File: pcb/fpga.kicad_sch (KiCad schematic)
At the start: 20 parts, among them J13 KB, J5 FPGA JTAG, J7 RAM cacheable, J8 ROM cacheable, U2 XC2S100TQ144, Y1 TXC-7C, Y2 GTXO-14T

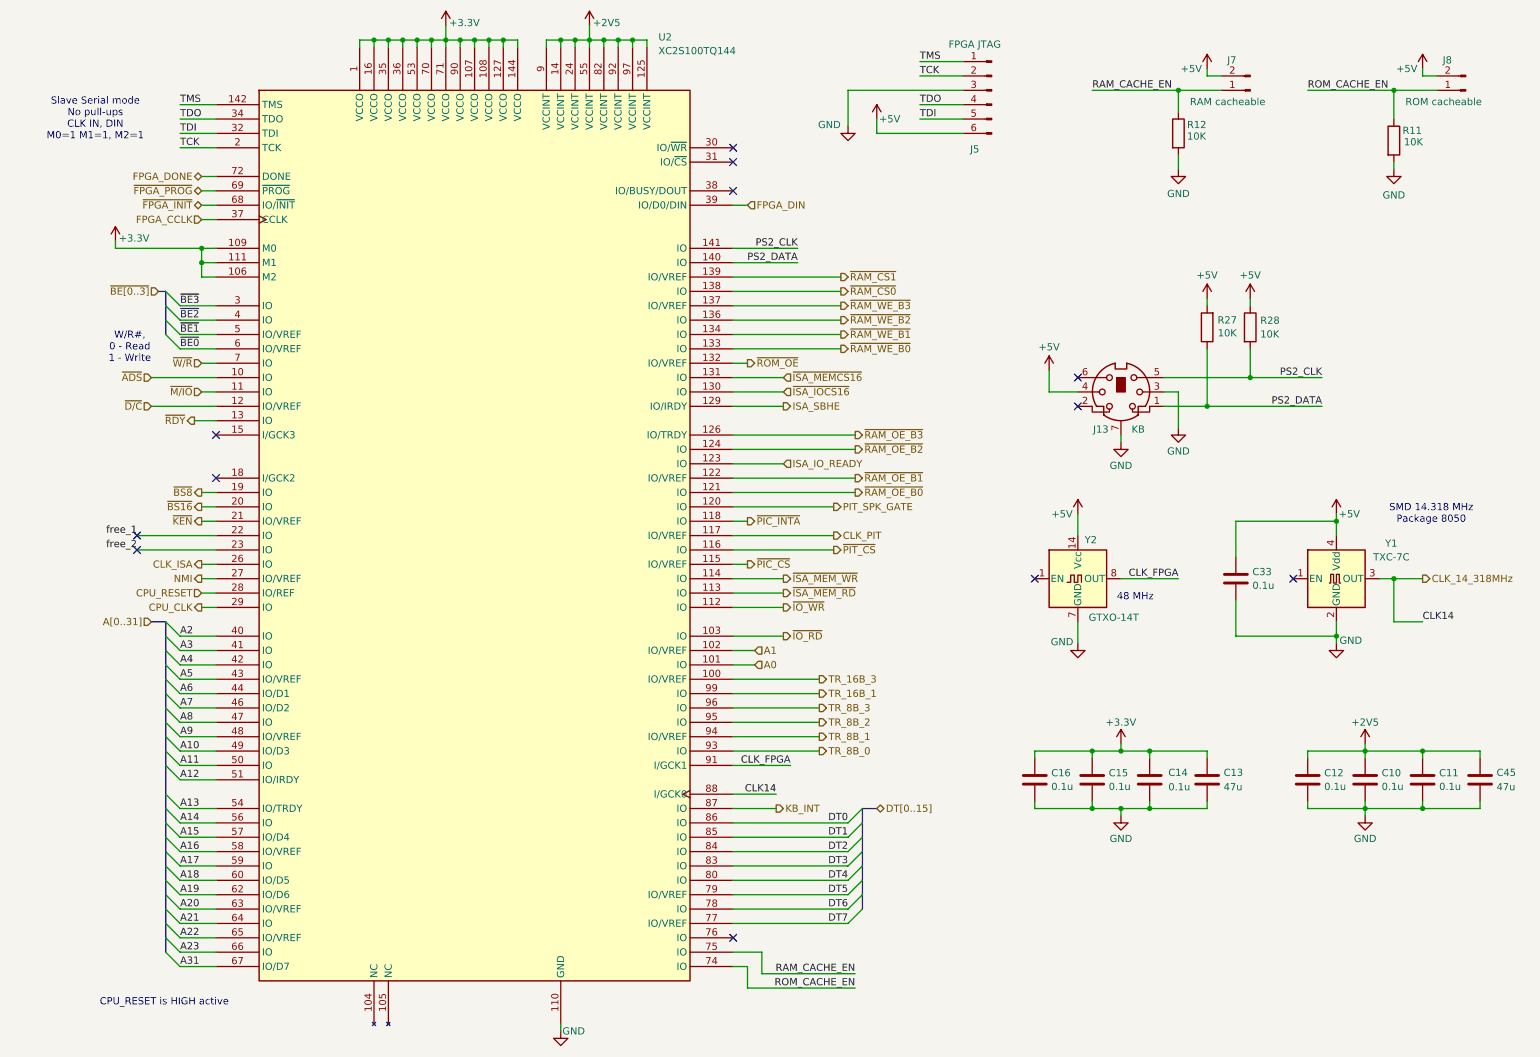
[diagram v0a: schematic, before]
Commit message: reshuffling FPGA diagram IO for better PCB routing, removed RAM/ROM CACHE_EN jumpers, 10 spare FPGA IO free. Replaced JTAG header with smaller probe points.
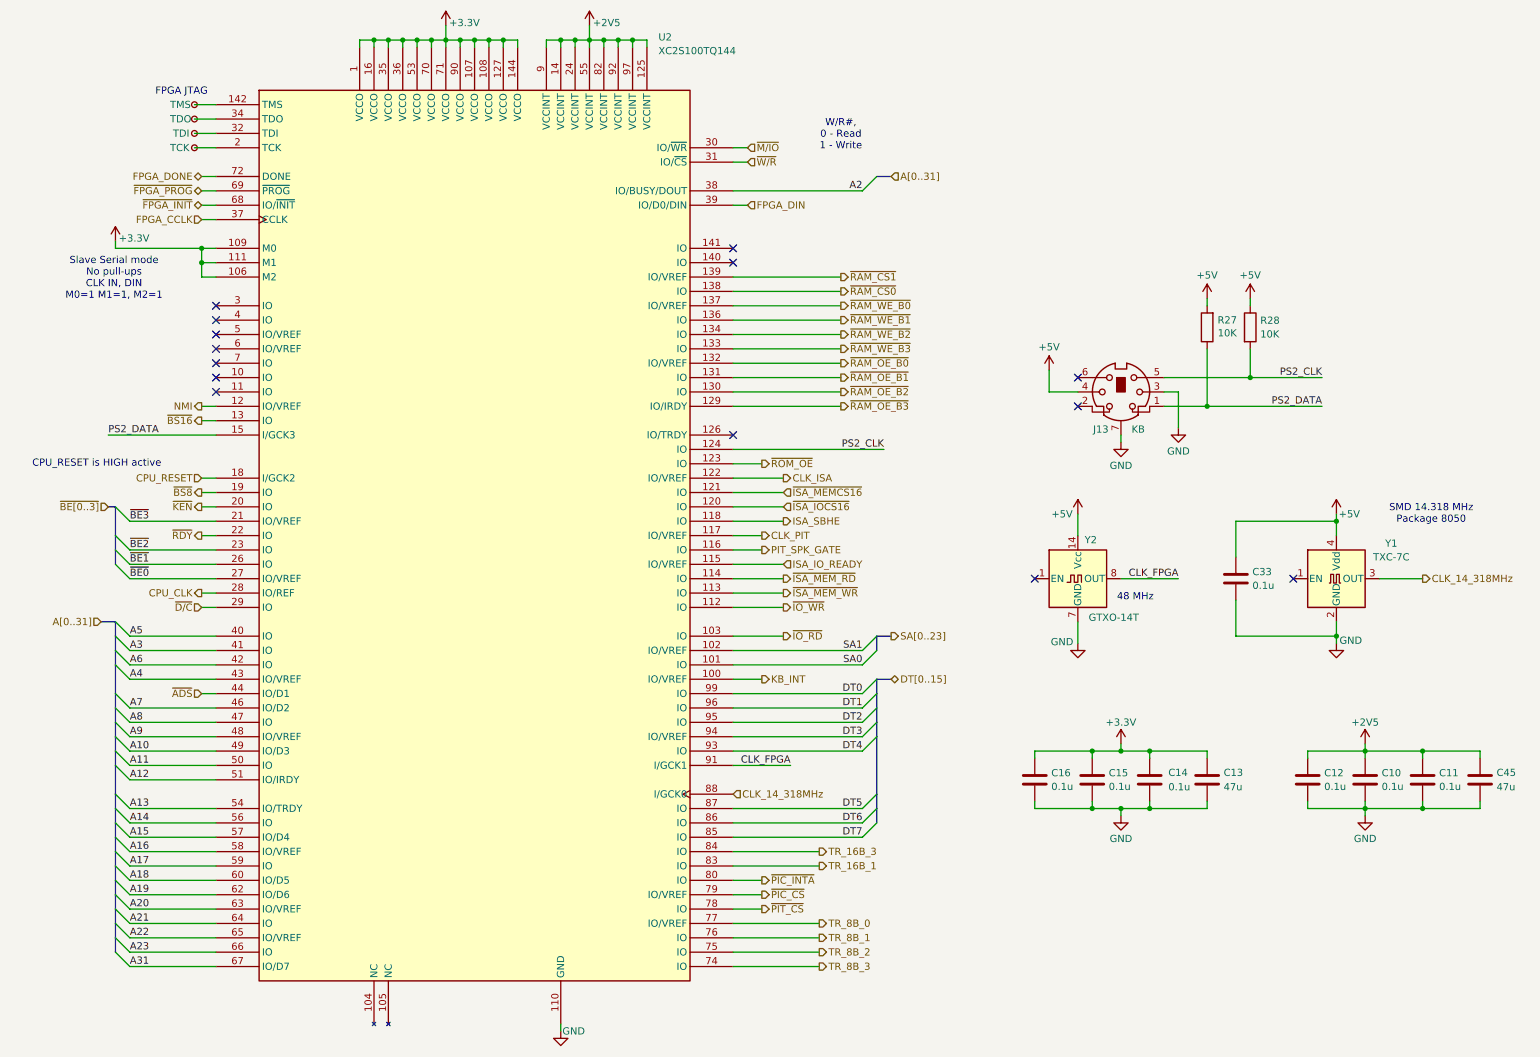
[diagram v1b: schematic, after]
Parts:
- removed J5: FPGA JTAG, Connector_PinHeader_2.54mm:PinHeader_1x06_P2.54mm_Vertical, symbol Connector:Conn_01x06_Pin
- removed J7: RAM cacheable, Connector_PinHeader_2.54mm:PinHeader_1x02_P2.54mm_Vertical, symbol Connector:Conn_01x02_Pin
- removed J8: ROM cacheable, Connector_PinHeader_2.54mm:PinHeader_1x02_P2.54mm_Vertical, symbol Connector:Conn_01x02_Pin
- removed R11, R12: 10K, Resistor_SMD:R_0805_2012Metric_Pad1.20x1.40mm_HandSolder, symbol Device:R
- added TP1: TDO, 486custom:TestPoint_Pad_D0.4mm, symbol Connector:TestPoint_Small
- added TP2: TDI, 486custom:TestPoint_Pad_D0.4mm, symbol Connector:TestPoint_Small
- added TP3: TMS, 486custom:TestPoint_Pad_D0.4mm, symbol Connector:TestPoint_Small
- added TP4: TCK, 486custom:TestPoint_Pad_D0.4mm, symbol Connector:TestPoint_Small
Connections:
- net RAM_CACHE_EN is gone; now on net TR_8B_2: U2.75 (IO)
- net ROM_CACHE_EN is gone; now on net TR_8B_3: U2.74 (IO)
- net free_1 is gone; now on net ~{RDY}: U2.22 (IO)
- net free_2 is gone; now on net ~{BE2}: U2.23 (IO)
- net A2: now also U2.38 (IO/BUSY/DOUT); no longer U2.40 (IO)
- net A4: now also U2.43 (IO/VREF); no longer U2.42 (IO)
- net A5: now also U2.40 (IO); no longer U2.43 (IO/VREF)
- net A6: now also U2.42 (IO); no longer U2.44 (IO/D1)
- net CLK_ISA: now also U2.122 (IO/VREF); no longer U2.26 (IO)
- net CPU_CLK: now also U2.28 (IO/REF); no longer U2.29 (IO)
- net CPU_RESET: now also U2.18 (I/GCK2); no longer U2.28 (IO/REF)
- net DT0: now also U2.99 (IO); no longer U2.86 (IO)
- net DT1: now also U2.96 (IO); no longer U2.85 (IO)
- net DT2: now also U2.95 (IO); no longer U2.84 (IO)
- net DT3: now also U2.94 (IO/VREF); no longer U2.83 (IO)
- net DT4: now also U2.93 (IO); no longer U2.80 (IO)
- net DT5: now also U2.87 (IO); no longer U2.79 (IO/VREF)
- net DT6: now also U2.86 (IO); no longer U2.78 (IO)
- net DT7: now also U2.85 (IO); no longer U2.77 (IO/VREF)
- net ISA_IO_READY: now also U2.115 (IO/VREF); no longer U2.123 (IO)
- net ISA_SBHE: now also U2.118 (IO); no longer U2.129 (IO/IRDY)
- net KB_INT: now also U2.100 (IO/VREF); no longer U2.87 (IO)
- net NMI: now also U2.12 (IO/VREF); no longer U2.27 (IO/VREF)
- net PIT_SPK_GATE: now also U2.116 (IO); no longer U2.120 (IO)
- net PS2_CLK: now also U2.124 (IO); no longer U2.141 (IO)
- net PS2_DATA: now also U2.15 (I/GCK3); no longer U2.140 (IO)
- net TR_16B_1: now also U2.83 (IO); no longer U2.99 (IO)
- net TR_16B_3: now also U2.84 (IO); no longer U2.100 (IO/VREF)
- net TR_8B_0: now also U2.77 (IO/VREF); no longer U2.93 (IO)
- net TR_8B_1: now also U2.76 (IO); no longer U2.94 (IO/VREF)
- net TR_8B_2: no longer U2.95 (IO)
- net TR_8B_3: no longer U2.96 (IO)
- net ~{ADS}: now also U2.44 (IO/D1); no longer U2.10 (IO)
- net ~{BE0}: now also U2.27 (IO/VREF); no longer U2.6 (IO/VREF)
- net ~{BE1}: now also U2.26 (IO); no longer U2.5 (IO/VREF)
- net ~{BE2}: no longer U2.4 (IO)
- net ~{BE3}: now also U2.21 (IO/VREF); no longer U2.3 (IO)
- net ~{BS16}: now also U2.13 (IO); no longer U2.20 (IO)
- net ~{D/C}: now also U2.29 (IO); no longer U2.12 (IO/VREF)
- net ~{ISA_IOCS16}: now also U2.120 (IO); no longer U2.130 (IO)
- net ~{ISA_MEMCS16}: now also U2.121 (IO); no longer U2.131 (IO)
- net ~{ISA_MEM_RD}: now also U2.114 (IO); no longer U2.113 (IO)
- net ~{ISA_MEM_WR}: now also U2.113 (IO); no longer U2.114 (IO)
- net ~{KEN}: now also U2.20 (IO); no longer U2.21 (IO/VREF)
- net ~{M/IO}: now also U2.30 (IO/~{WR}); no longer U2.11 (IO)
- net ~{PIC_CS}: now also U2.79 (IO/VREF); no longer U2.115 (IO/VREF)
- net ~{PIC_INTA}: now also U2.80 (IO); no longer U2.118 (IO)
- net ~{PIT_CS}: now also U2.78 (IO); no longer U2.116 (IO)
- net ~{RAM_OE_B0}: now also U2.132 (IO/VREF); no longer U2.121 (IO)
- net ~{RAM_OE_B1}: now also U2.131 (IO); no longer U2.122 (IO/VREF)
- net ~{RAM_OE_B2}: now also U2.130 (IO); no longer U2.124 (IO)
- net ~{RAM_OE_B3}: now also U2.129 (IO/IRDY); no longer U2.126 (IO/TRDY)
- net ~{RAM_WE_B0}: now also U2.137 (IO/VREF); no longer U2.133 (IO)
- net ~{RAM_WE_B1}: now also U2.136 (IO); no longer U2.134 (IO)
- net ~{RAM_WE_B2}: now also U2.134 (IO); no longer U2.136 (IO)
- net ~{RAM_WE_B3}: now also U2.133 (IO); no longer U2.137 (IO/VREF)
- net ~{RDY}: no longer U2.13 (IO)
- net ~{ROM_OE}: now also U2.123 (IO); no longer U2.132 (IO/VREF)
- net ~{W/R}: now also U2.31 (IO/~{CS}); no longer U2.7 (IO)
- net A0 renamed SA0
- net A1 renamed SA1
- net TCK: no longer names the net of U2.2 (TCK)
- net TCK: now also TP4.1
- net TDI: no longer names the net of U2.32 (TDI)
- net TDI: now also TP2.1
- net TDO: no longer names the net of U2.34 (TDO)
- net TDO: now also TP1.1
- net TMS: no longer names the net of U2.142 (TMS)
- net TMS: now also TP3.1
- no-connect marks 12 -> 14
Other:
- note added: "FPGA JTAG"

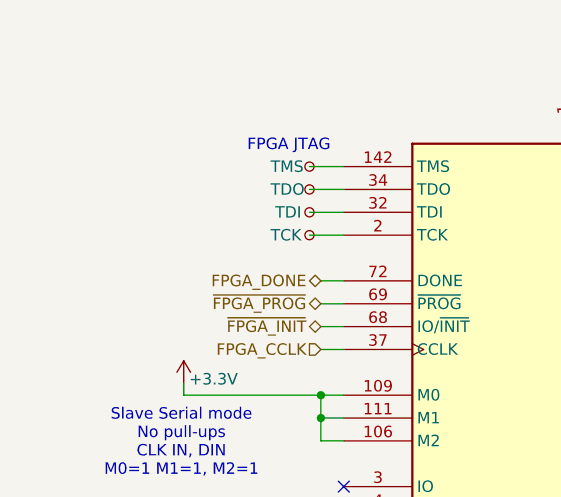
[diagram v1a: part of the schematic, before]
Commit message: fpga diagram extra JTAG ground point
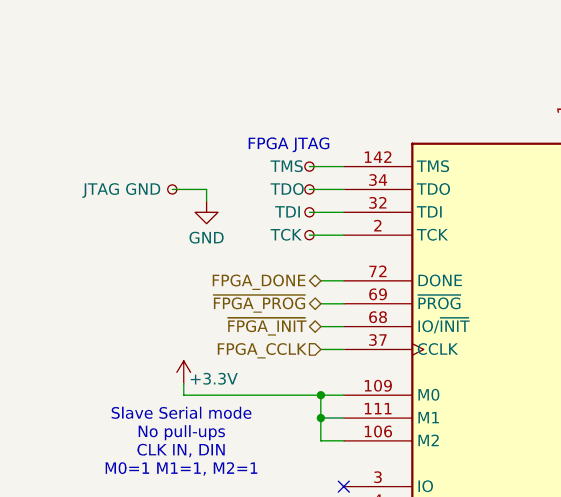
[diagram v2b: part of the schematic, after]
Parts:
- added TP5: JTAG GND, 486custom:TestPoint_Pad_D0.4mm, symbol Connector:TestPoint_Small
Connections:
- net GND: now also TP5.1
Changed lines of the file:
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@@
 	(wire
 		(pts
+			(xy 33.02 33.02) (xy 33.02 34.29)
+		)
+		(stroke
+			(width 0)
+			(type default)
+		)
+	)
+	(wire
+		(pts
 			(xy 223.52 144.78) (xy 223.52 146.05)
 		)
@@
 	(wire
 		(pts
+			(xy 29.21 33.02) (xy 33.02 33.02)
+		)
+		(stroke
+			(width 0)
+			(type default)
+		)
+	)
+	(wire
+		(pts
 			(xy 114.3 19.05) (xy 114.3 20.32)
 		)
@@
 	)
 	(symbol
+		(lib_id "Connector:TestPoint_Small")
+		(at 29.21 33.02 0)
+		(unit 1)
+		(exclude_from_sim no)
+		(in_bom yes)
+		(on_board yes)
+		(dnp no)
+		(property "Reference" "TP5"
+			(at 22.86 33.02 0)
+			(effects
+				(font
+					(size 1.27 1.27)
+				)
+				(justify left)
+				(hide yes)
+			)
+		)
+		(property "Value" "JTAG GND"
+			(at 19.304 33.02 0)
+			(effects
+				(font
+					(size 1.27 1.27)
+				)
+				(justify left)
+			)
+		)
+		(property "Footprint" "486custom:TestPoint_Pad_D0.4mm"
+			(at 34.29 33.02 0)
+			(effects
+				(font
+					(size 1.27 1.27)
+				)
+				(hide yes)
+			)
+		)
+		(property "Datasheet" "~"
+			(at 34.29 33.02 0)
+			(effects
+				(font
+					(size 1.27 1.27)
+				)
+				(hide yes)
+			)
+		)
+		(property "Description" "test point"
+			(at 29.21 33.02 0)
+			(effects
+				(font
+					(size 1.27 1.27)
+				)
+				(hide yes)
+			)
+		)
+		(pin "1"
+		)
+		(instances
+			(project "homebrew_486"
+				(path "/360fb3b9-a21a-4226-8954-bf45cf17bb35/49c3128c-49f0-451c-bde3-bf7412e8a8c9"
+					(reference "TP5")
+					(unit 1)
+				)
+			)
+		)
+	)
+	(symbol
 		(lib_id "power:+2V5")
 		(at 114.3 16.51 0)
@@
 					(unit 1)
 				)
+			)
+		)
+	)
+	(symbol
+		(lib_id "power:GND")
+		(at 33.02 34.29 0)
+		(unit 1)
+		(exclude_from_sim no)
+		(in_bom yes)
+		(on_board yes)
+		(dnp no)
+		(fields_autoplaced yes)
+		(property "Reference" "#PWR085"
+			(at 33.02 40.64 0)
+			(effects
+				(font
+					(size 1.27 1.27)
+				)
+				(hide yes)
+			)
+		)
+		(property "Value" "GND"
+			(at 33.02 38.4231 0)
+			(effects
+				(font
+					(size 1.27 1.27)
+				)
+			)
+		)
+		(property "Footprint" ""
+			(at 33.02 34.29 0)
+			(effects
+				(font
+					(size 1.27 1.27)
+				)
+				(hide yes)
+			)
+		)
+		(property "Datasheet" ""
+			(at 33.02 34.29 0)
+			(effects
+				(font
+					(size 1.27 1.27)
+				)
+				(hide yes)
+			)
+		)
+		(property "Description" "Power symbol creates a global label with name \"GND\" , ground"
+			(at 33.02 34.29 0)
+			(effects
+				(font
+					(size 1.27 1.27)
+				)
+				(hide yes)
+			)
+		)
+		(pin "1"
+		)
+		(instances
+			(project "homebrew_486"
+				(path "/360fb3b9-a21a-4226-8954-bf45cf17bb35/49c3128c-49f0-451c-bde3-bf7412e8a8c9"
+					(reference "#PWR085")
+					(unit 1)
+				)

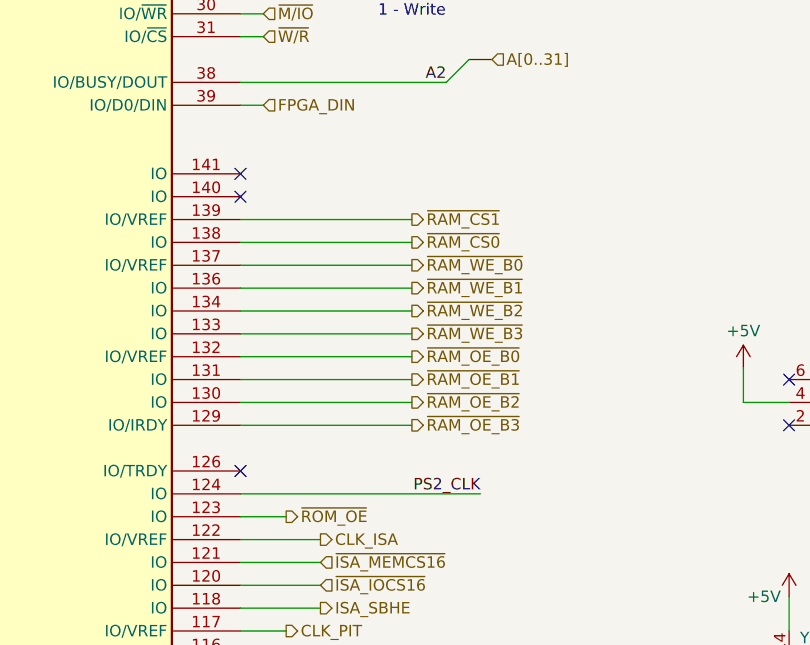
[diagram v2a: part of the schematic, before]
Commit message: few more free IO pads exposed
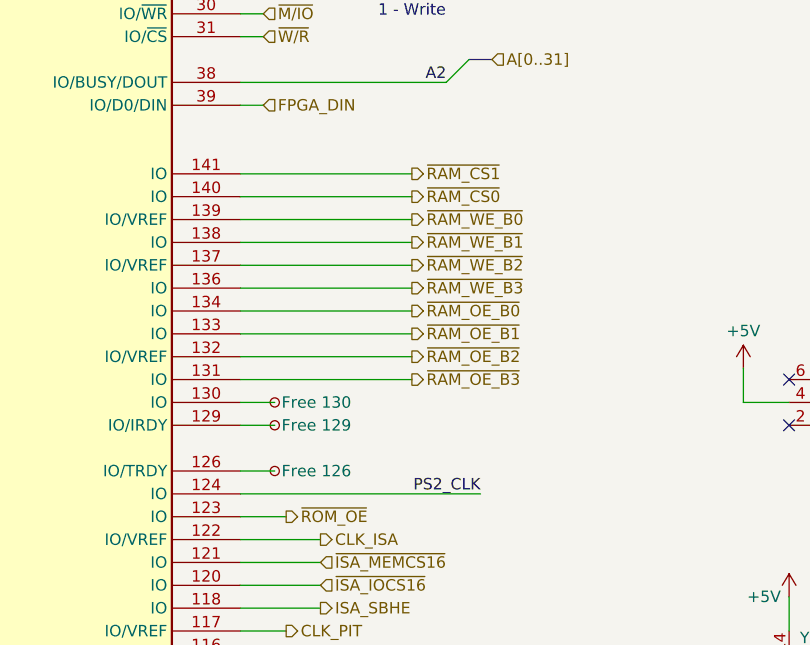
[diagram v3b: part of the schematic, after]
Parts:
- added TP15: Free 126, 486custom:TestPoint_Pad_D0.4mm, symbol Connector:TestPoint_Small
- added TP16: Free 130, 486custom:TestPoint_Pad_D0.4mm, symbol Connector:TestPoint_Small
- added TP17: Free 129, 486custom:TestPoint_Pad_D0.4mm, symbol Connector:TestPoint_Small
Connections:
- net ~{RAM_CS0}: now also U2.140 (IO); no longer U2.138 (IO)
- net ~{RAM_CS1}: now also U2.141 (IO); no longer U2.139 (IO/VREF)
- net ~{RAM_OE_B0}: now also U2.134 (IO); no longer U2.132 (IO/VREF)
- net ~{RAM_OE_B1}: now also U2.133 (IO); no longer U2.131 (IO)
- net ~{RAM_OE_B2}: now also U2.132 (IO/VREF); no longer U2.130 (IO)
- net ~{RAM_OE_B3}: now also U2.131 (IO); no longer U2.129 (IO/IRDY)
- net ~{RAM_WE_B0}: now also U2.139 (IO/VREF); no longer U2.137 (IO/VREF)
- net ~{RAM_WE_B1}: now also U2.138 (IO); no longer U2.136 (IO)
- net ~{RAM_WE_B2}: now also U2.137 (IO/VREF); no longer U2.134 (IO)
- net ~{RAM_WE_B3}: now also U2.136 (IO); no longer U2.133 (IO)
- net at U2.126 (IO/TRDY): now also TP15.1
- new net: TP16.1, U2.130 (IO)
- new net: TP17.1, U2.129 (IO/IRDY)
- no-connect marks 14 -> 11
